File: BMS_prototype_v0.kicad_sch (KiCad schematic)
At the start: 44 parts, among them J1 Conn_02x12_Odd_Even, J2 Conn_01x13_Pin, J3 Conn_01x02_Pin, J4 Conn_01x02_Pin, SW1 SW_DIP_x01

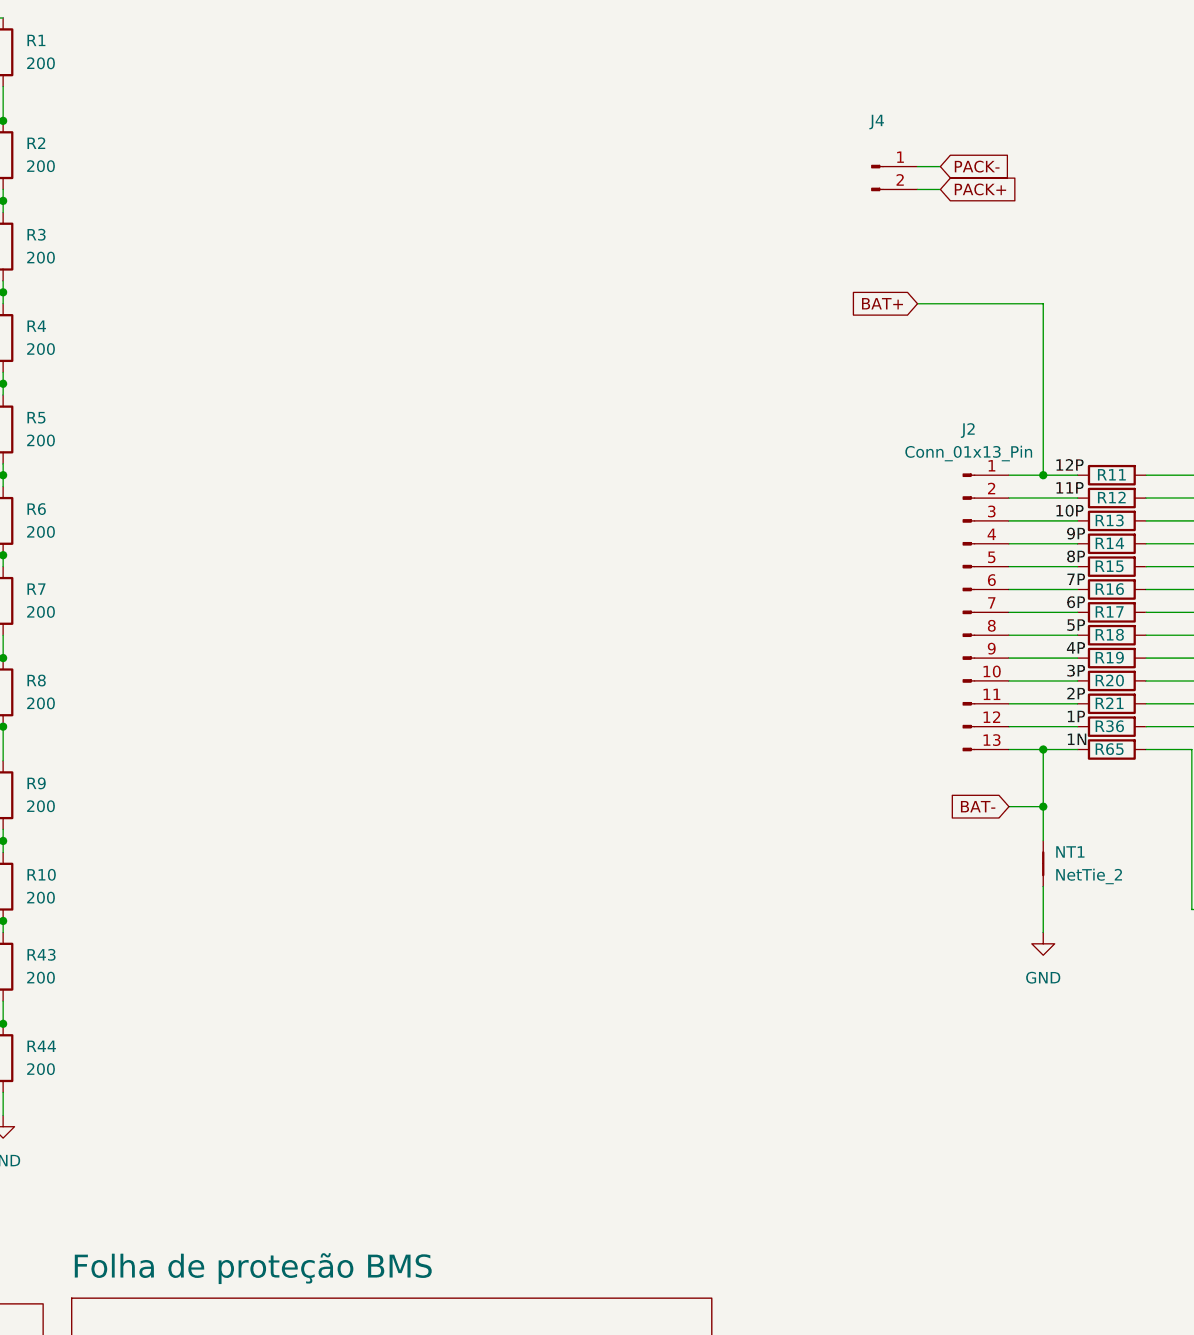
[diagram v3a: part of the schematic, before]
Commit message: posiciona testpoints
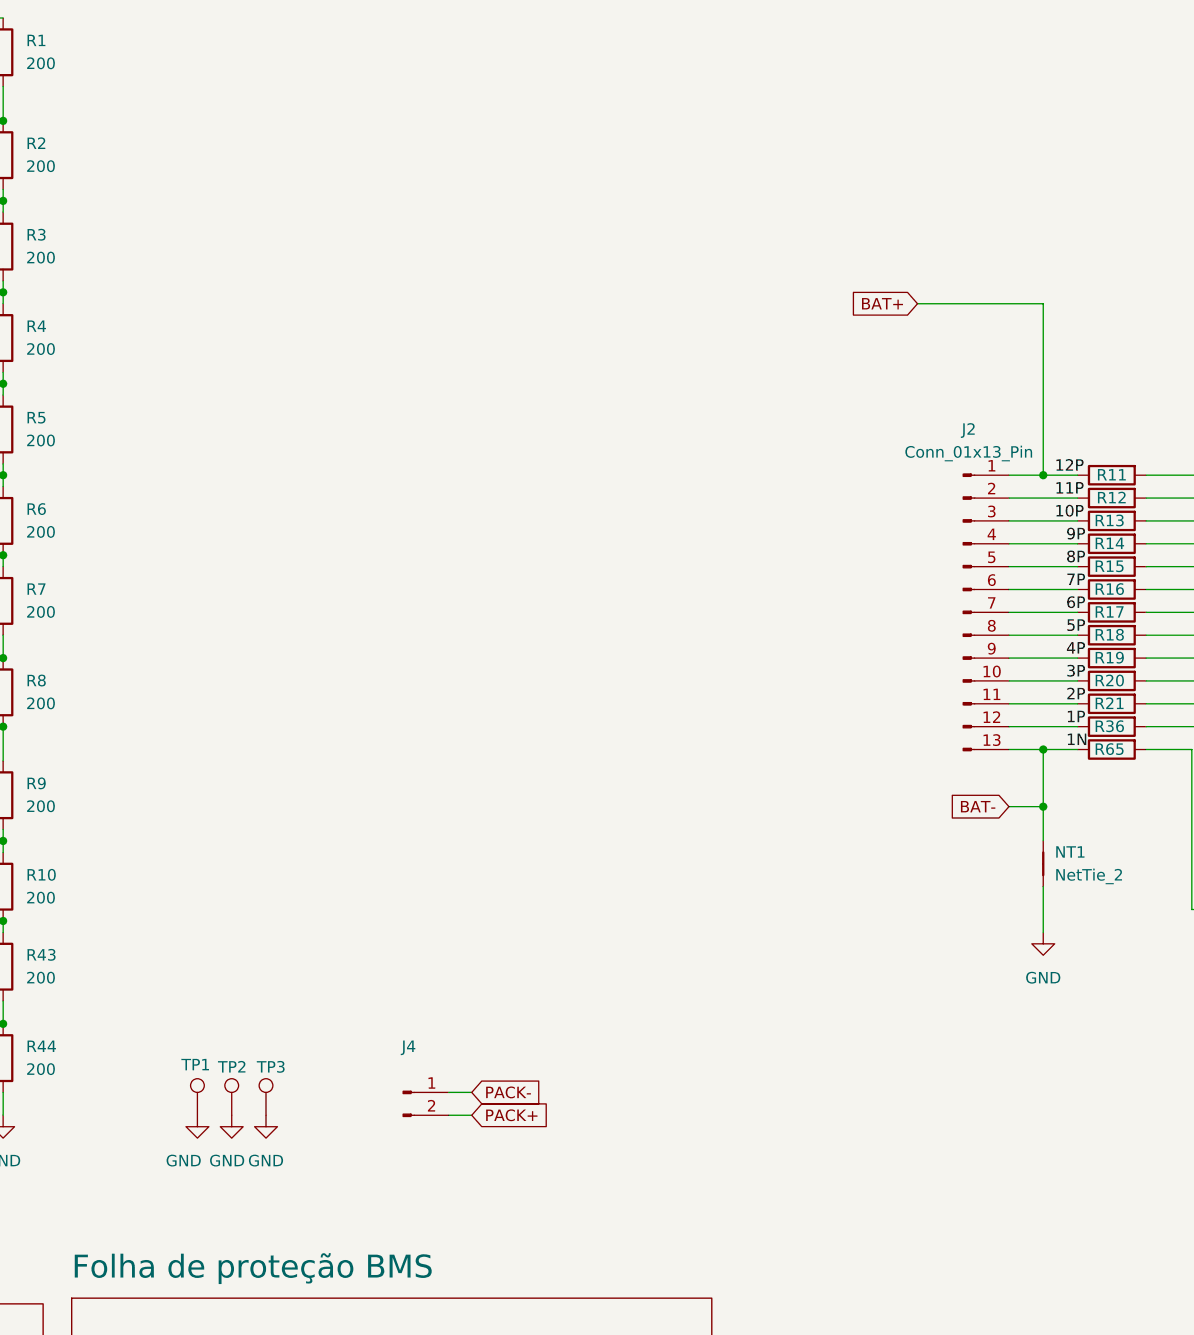
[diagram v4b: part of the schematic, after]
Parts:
- added TP1, TP2, TP3: TestPoint, TestPoint:TestPoint_Pad_3.0x3.0mm, symbol Connector:TestPoint
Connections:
- net GND: now also TP1.1, TP2.1, TP3.1
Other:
- moved on the sheet: J4
